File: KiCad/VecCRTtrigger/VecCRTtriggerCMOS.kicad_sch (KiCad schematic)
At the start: 14 parts, among them J1 Conn_01x03_Male, J2 Conn_01x03_Male, Q1 2N7000, U1 4093

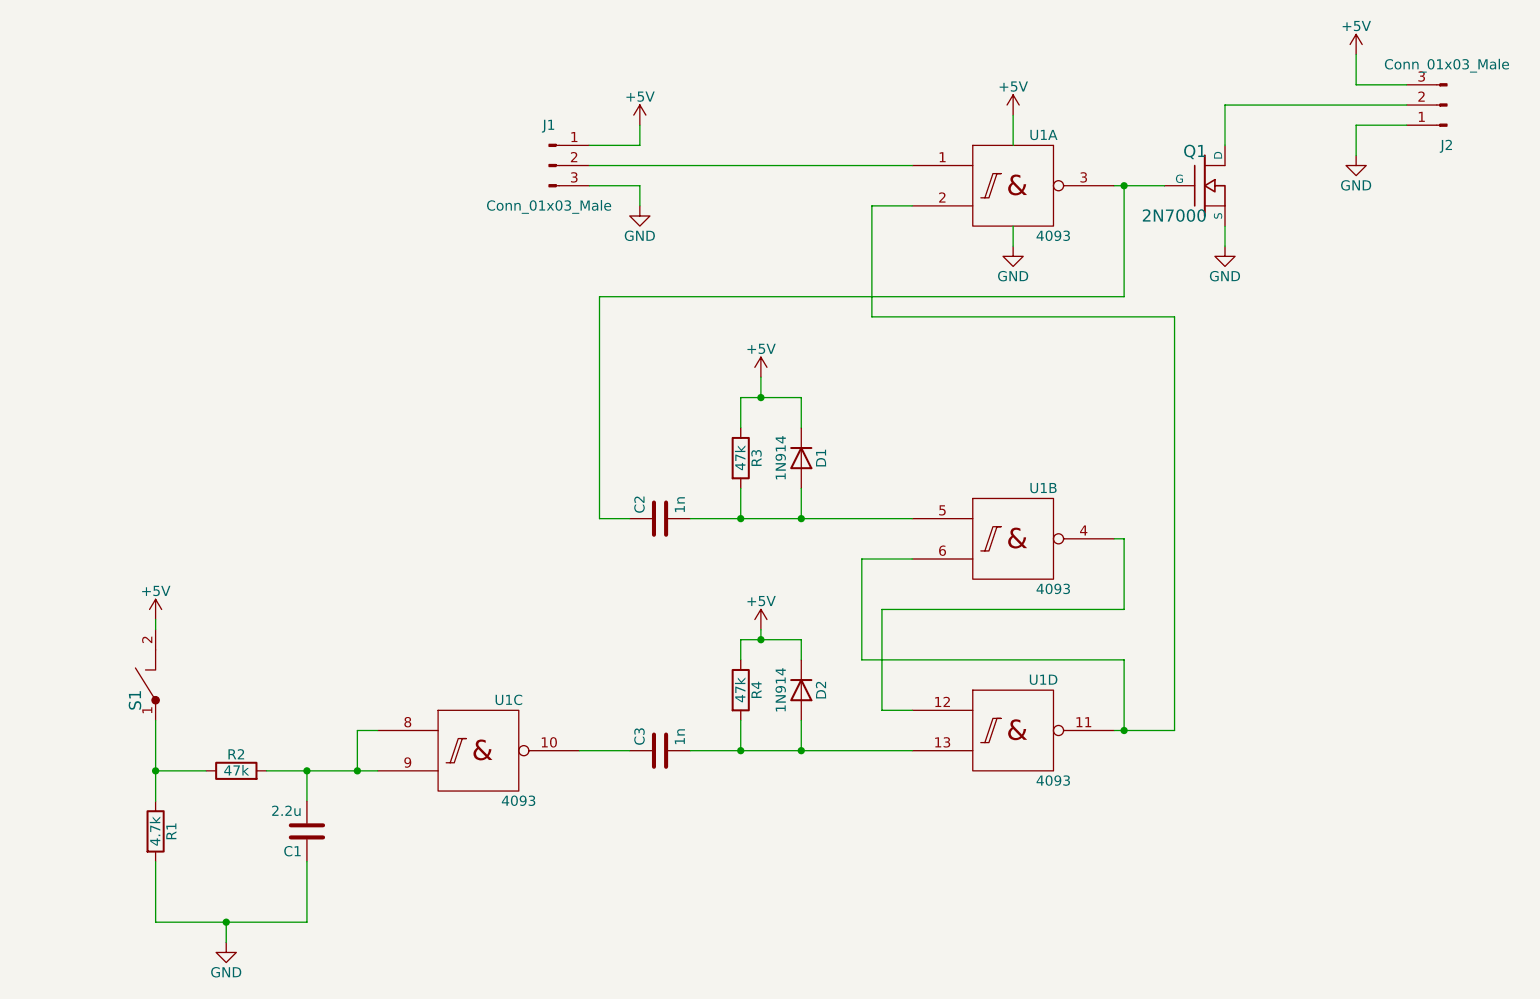
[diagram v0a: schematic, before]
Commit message: Trigger switch with CMOS
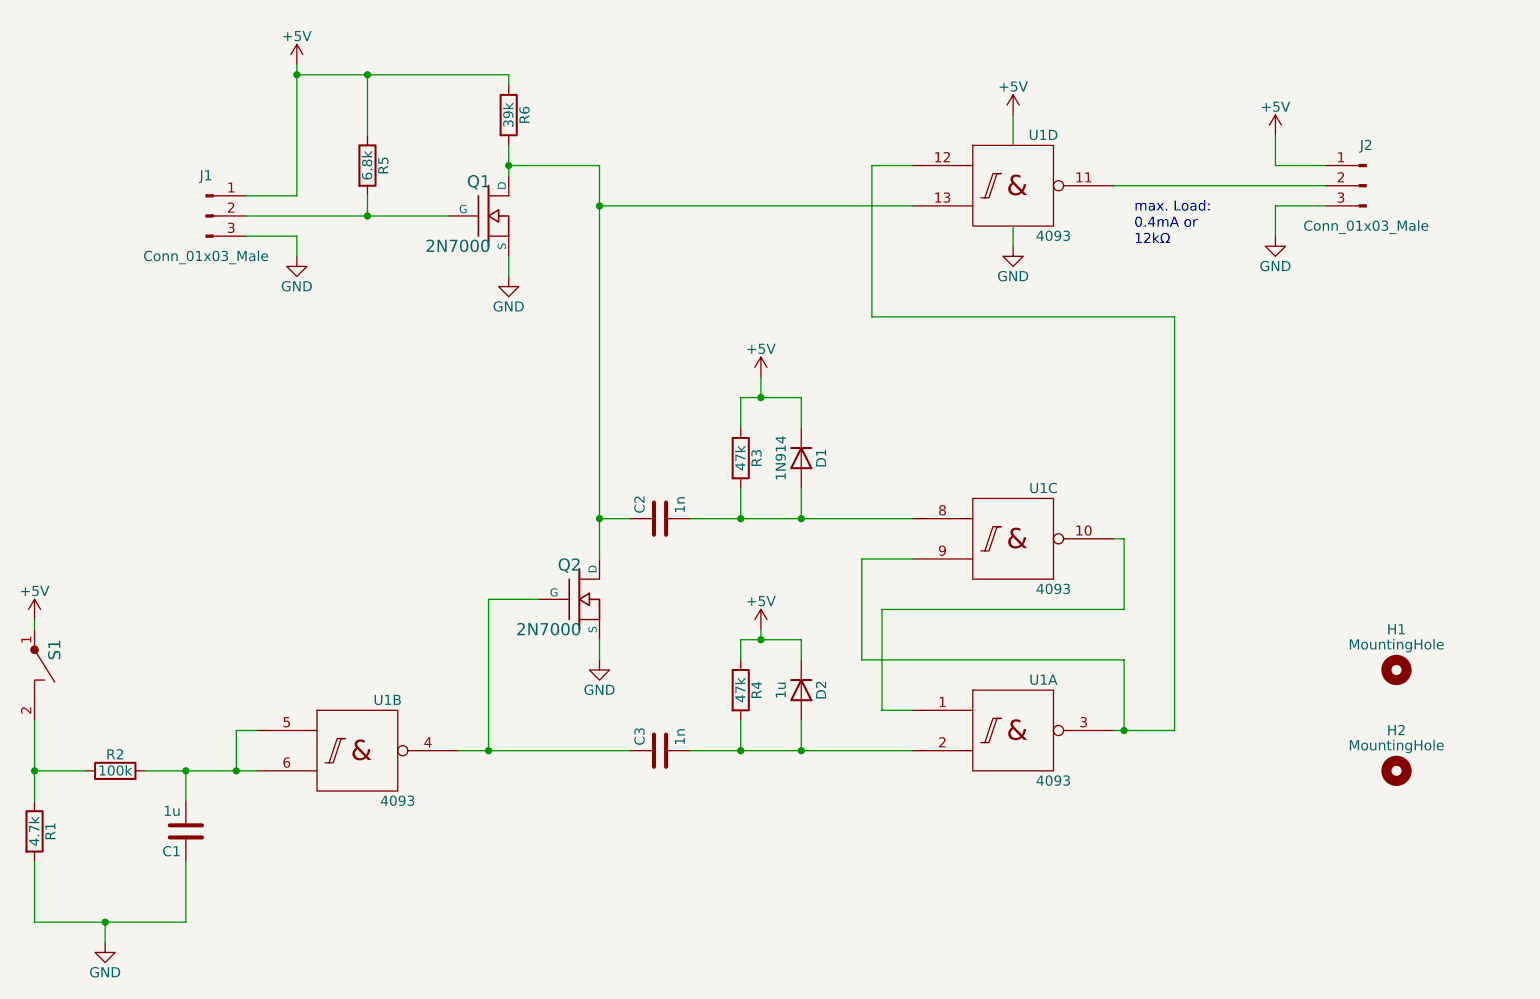
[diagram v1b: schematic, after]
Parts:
- added H1, H2: MountingHole, MountingHole:MountingHole_2.5mm, symbol Mechanical:MountingHole
- added Q2: 2N7000, RG:FETsgd_inline, symbol rg:2N7000
- added R5: 6.8k, RG:R4-2, symbol Device:R
- added R6: 39k, RG:R4-2, symbol Device:R
- C1: value 2.2u -> 1u; footprint (none) -> RG:C2-2_liegend
- C2, C3: footprint (none) -> RG:C2-2
- D1: footprint Diode_THT:D_DO-35_SOD27_P7.62mm_Horizontal -> RG:D3
- D2: value 1N914 -> 1u; footprint Diode_THT:D_DO-35_SOD27_P7.62mm_Horizontal -> RG:D3
- J1, J2: footprint (none) -> RG:Pins_3
- R1, R3, R4: footprint (none) -> RG:R4-2
- R2: value 47k -> 100k; footprint (none) -> RG:R4-2
- S1: footprint (none) -> RG:Pins_2
- U1: footprint (none) -> RG:DIP-14_W7.62mm_LongPads
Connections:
- net +5V: now also J2.1 (Pin_1), S1.1, R5.1, R6.1; no longer J2.3 (Pin_3), S1.2
- net GND: now also J2.3 (Pin_3), Q2.S; no longer J2.1 (Pin_1)
- net at R1.1, R2.1: now also S1.2; no longer S1.1
- net at C3.1: now also U1.4, Q2.G; no longer U1.10
- net at C3.2, D2.2 (A), R4.2: now also U1.2; no longer U1.13
- net at C2.2, D1.2 (A), R3.2: now also U1.8; no longer U1.5
- net at Q1.D: now also C2.1, U1.13, Q2.D, R6.2; no longer J2.2 (Pin_2)
- net at J1.2 (Pin_2): now also Q1.G, R5.2; no longer U1.1
- net at U1.12: now also U1.3, U1.9; no longer U1.4
- net at C1.2, R2.2: now also U1.5, U1.6; no longer U1.8, U1.9
- new net: U1.1, U1.10
- new net: J2.2 (Pin_2), U1.11
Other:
- note added: "max. Load: 0.4mA or 12kΩ"
- moved on the sheet: C1, J1, J2, Q1, R1, R2, S1, U1A, U1B, U1C, U1D
